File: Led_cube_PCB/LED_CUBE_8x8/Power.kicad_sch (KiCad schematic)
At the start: 13 parts, among them IC28 TPS562202DRLR, J1 1984963

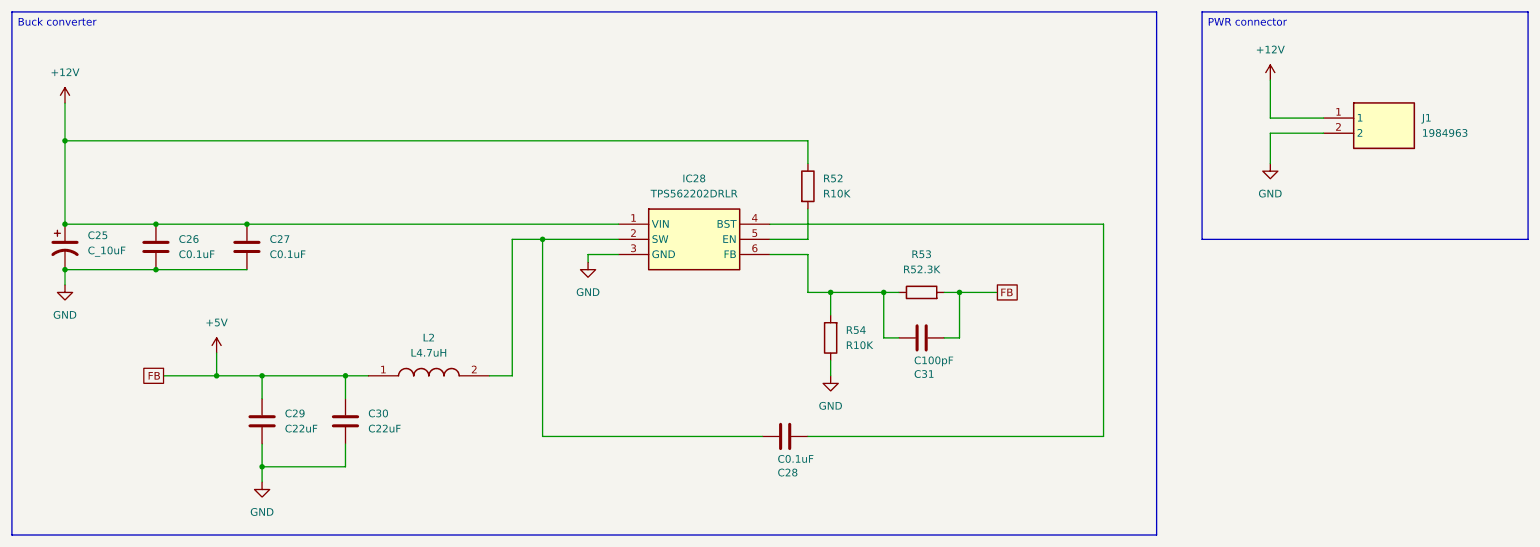
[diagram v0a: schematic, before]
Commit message: Added test points and solder jumpers
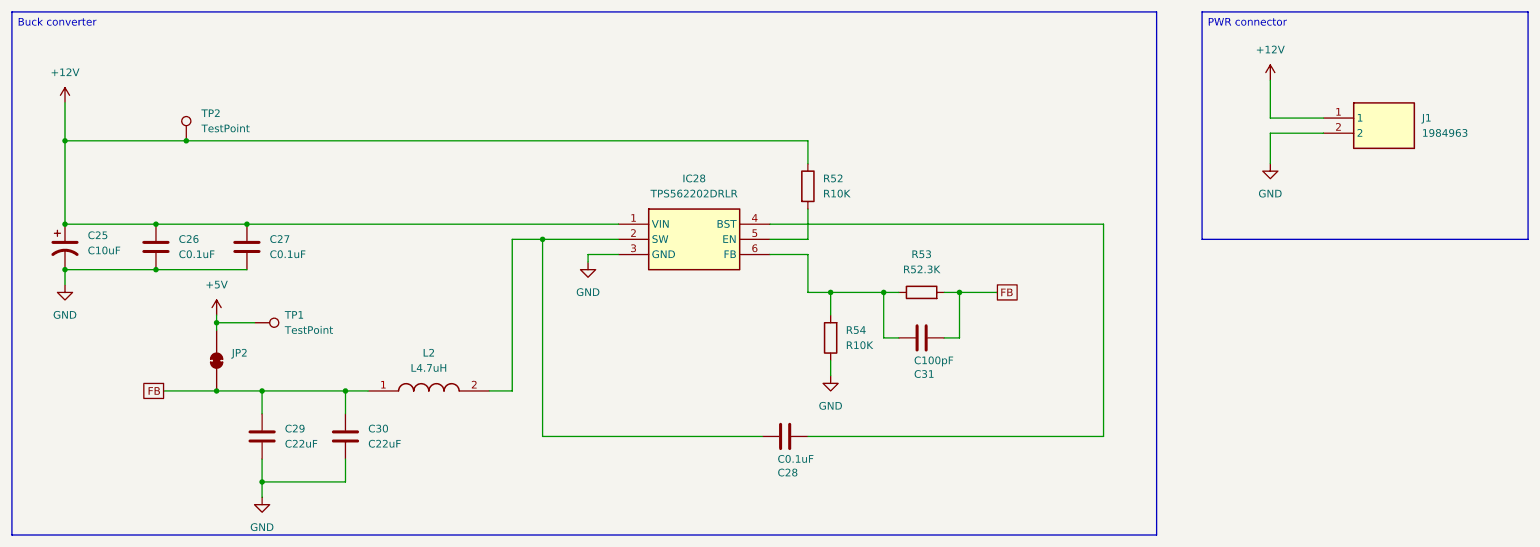
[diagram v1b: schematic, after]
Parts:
- added JP2: SolderJumper_2_Bridged, Jumper:SolderJumper-2_P1.3mm_Open_RoundedPad1.0x1.5mm, symbol Jumper:SolderJumper_2_Bridged
- added TP1, TP2: TestPoint, TestPoint:TestPoint_Pad_D2.0mm, symbol Connector:TestPoint
- C25: value C_10uF -> C10uF
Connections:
- net +12V: now also TP2.1
- net +5V: now also JP2.2 (B), TP1.1; no longer C29.1, C30.1, C31.1, L2.1, R53.2
- new net FB: C29.1, C30.1, C31.1, JP2.1 (A), L2.1, R53.2
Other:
- moved on the sheet: C29, C30, L2
